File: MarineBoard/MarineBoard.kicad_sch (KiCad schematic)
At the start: 161 parts, among them CN1 MKDSN 1,5/ 2-5,08, CN2 MKDSN 1,5/ 2-5,08, CN3 SM04B-SRSS-TB (LF)(SN), CN4 BM10B-GHS-TBT, J1 USB_C_Receptacle_USB2.0_16P, Q2 S8050, Q3 S8050, Q4 BUK762R4-60E, U1 SY8089A1AAC, U11 SN65HVD230DR, U12 DB125-3.5-3P-GN-S, U13 DB125-3.5-3P-GN-S, U14 PC817C-S, U16 PC817C-S, U17 PC817C-S, U18 INA226, U19 INA226, U2 INA226, U21 PC817C-S, U22 SN74LVC1G14DBVR, U23 MCP1407-E/MF_C640313, U3 TPS5430DDA, U4 DB125-3.5-2P-GN-S, U5 DB125-3.5-2P-GN-S, U6 DB125-3.5-2P-GN-S, U7 DB125-3.5-3P-GN-S, U8 ESP32-S3-WROOM-2-N32R16V, U9 DB125-3.5-3P-GN-S

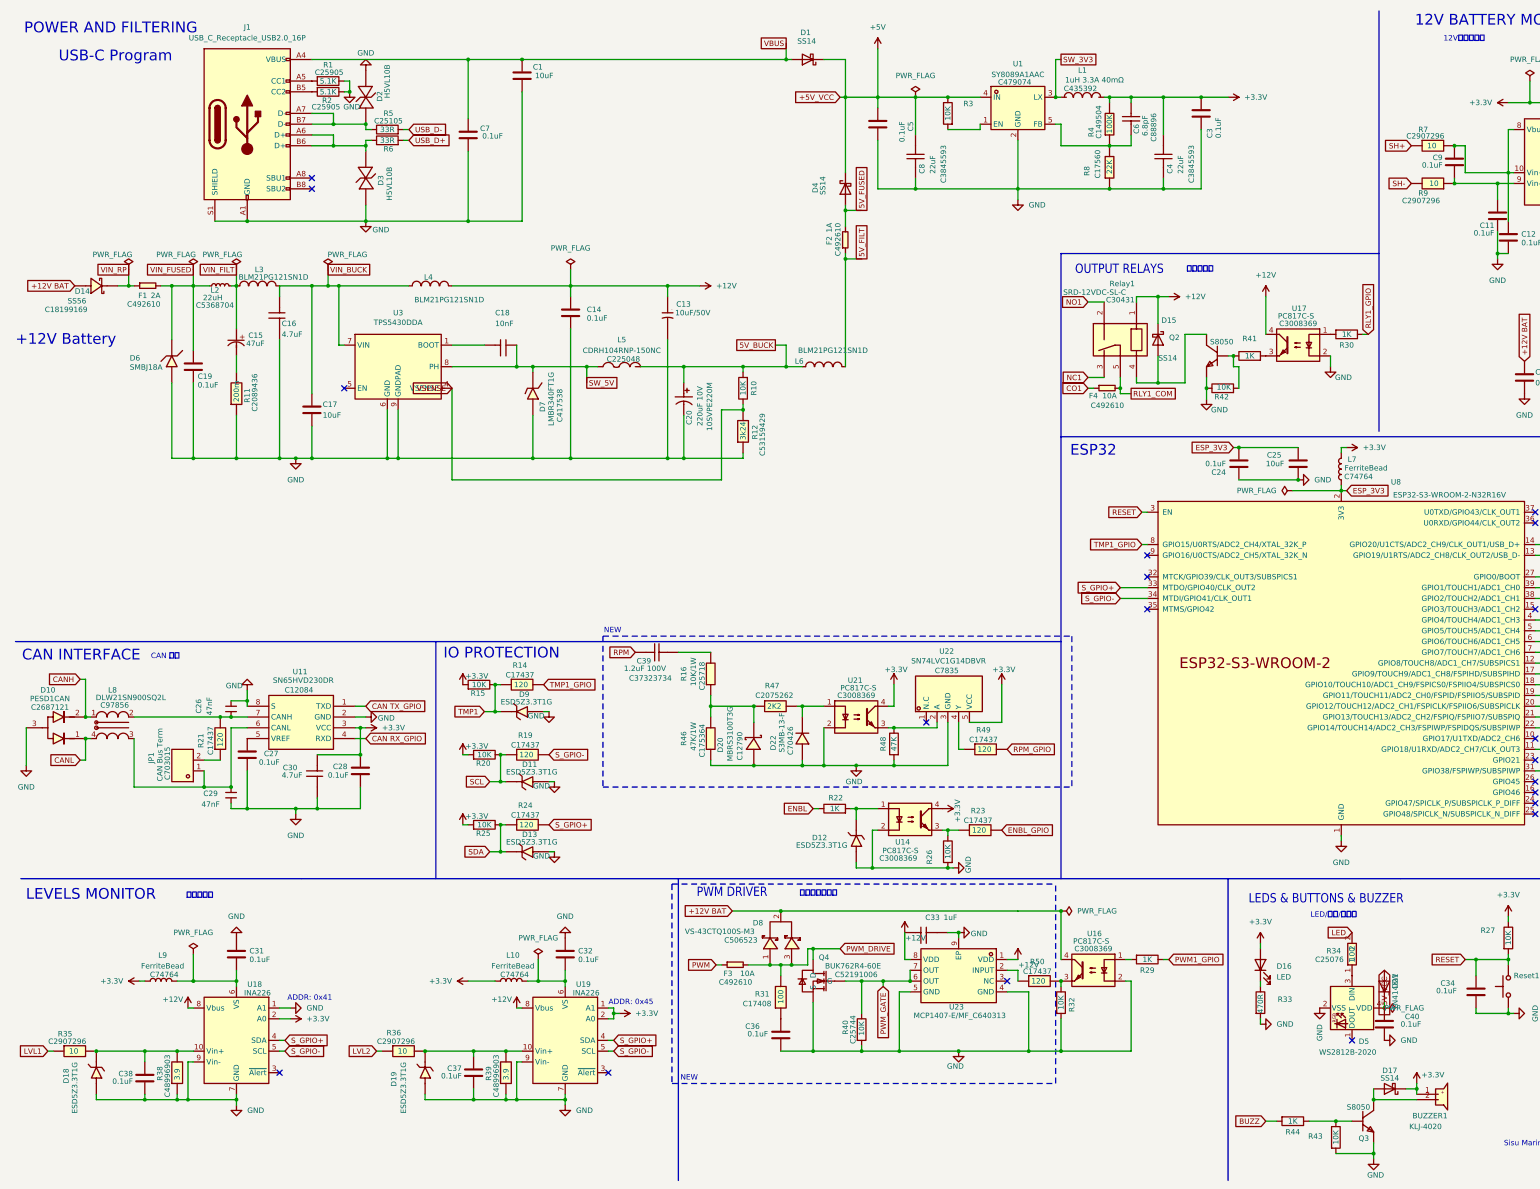
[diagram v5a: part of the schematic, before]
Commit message: MarineBoard: enclosure, PCBWay delivery, 5-unit BOM (#194)
Enclosure: printed PA12 box 129.4 x 107.9 x 44 mm, built by a parametric
FreeCAD script (enclosure/make_enclosure.py; fit_board.py checks the KiCad
board STEP against it). IP67 panel connectors with engraved legends
(EW-LP20 power/PWM, M12-5 CAN, 12G for TMP/RPM/ENBL, relay, shunt,
levels), 2 mm silicone-cord seal, D5 light pipe, 4 x M3x6 board and
4 x M3x10 lid screws, no USB opening (flash before boxing, then OTA).
STEP + STL exports, FreeCAD docs, render, and the PCBWay print/parts
order sheet. Documented in Technical Specs -> Enclosure; README,
INSTALLATION section 8.3 and Technical Specifications point to it.

Also: PCBWay's 15 Aug delivery package (design files, CAM, the earlier
enclosure, now marked superseded), the connector purchase list, and
the 5-unit assembly BOM. Order numbers are kept out of the file names.
Board BOM: real part numbers for generic parts (BLM21PG331SN1D,
KT-0603R, MCP1407-E/MF); production files regenerated; no copper change.
FreeCAD *.FCBak backups ignored. Project Claude permissions updated.

Signal K plugin configs stay uncommitted (local MQTT credentials).

Co-Authored-By: Claude Opus 5.5 <noreply@anthropic.com>
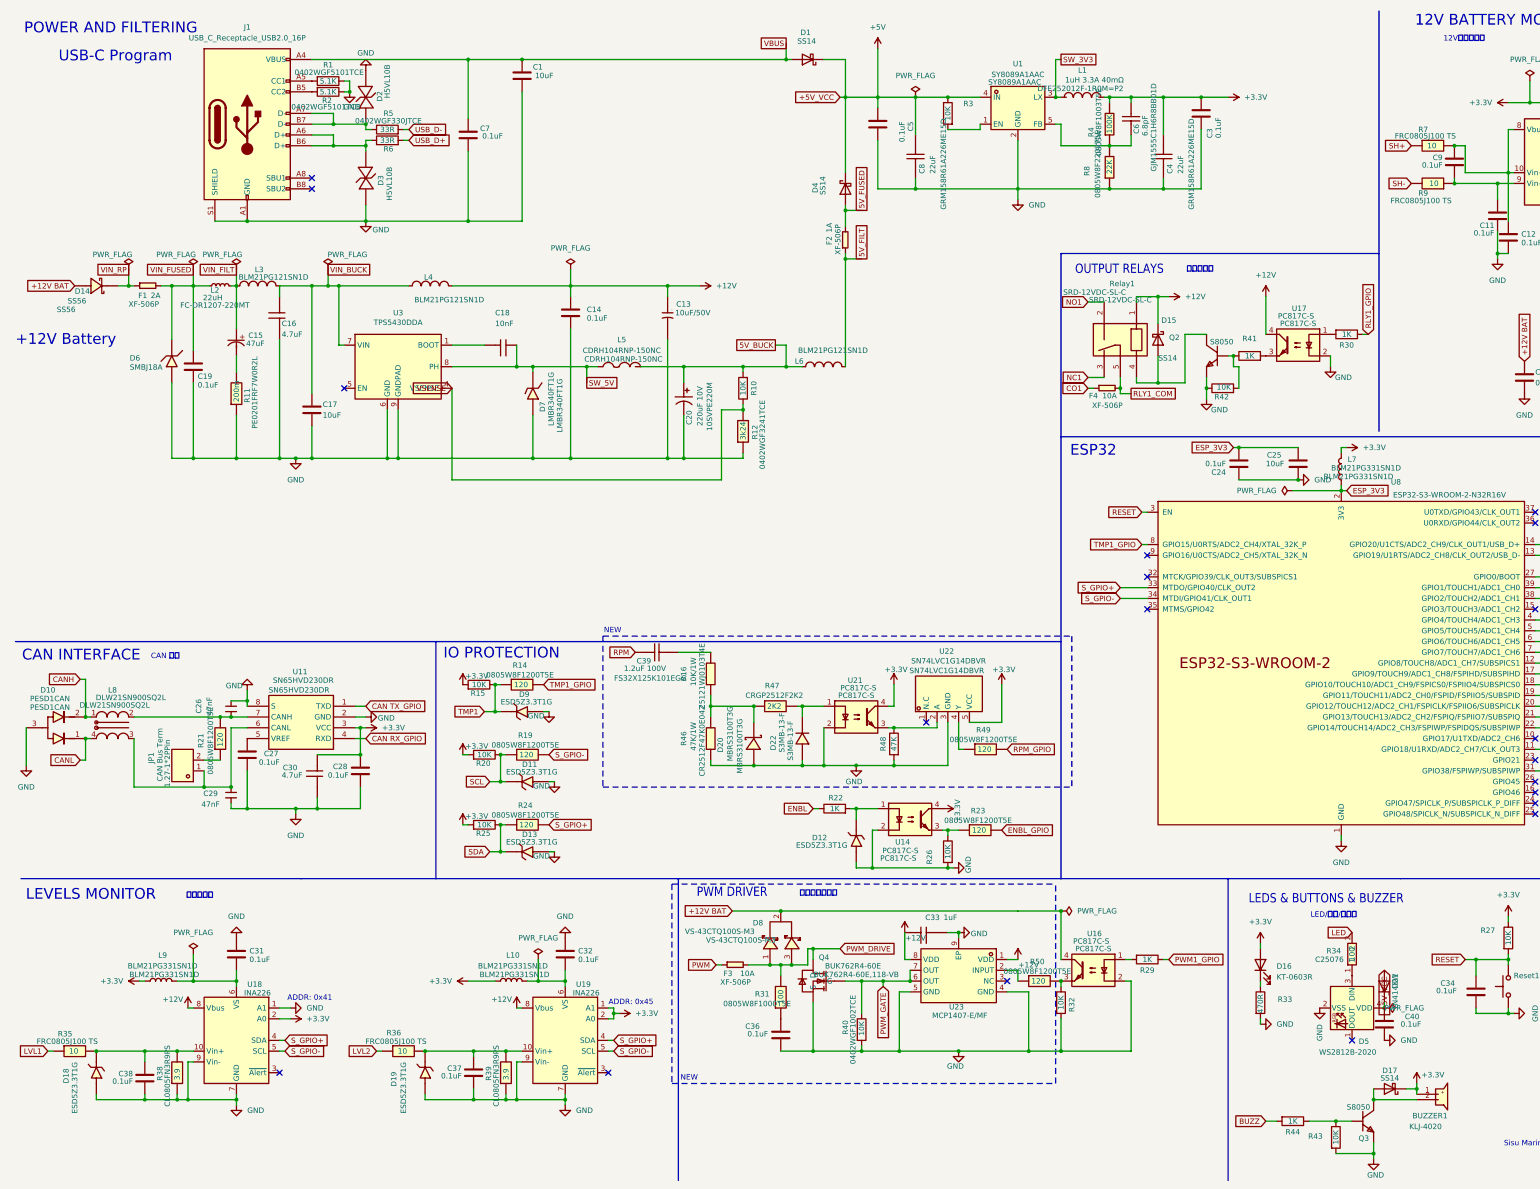
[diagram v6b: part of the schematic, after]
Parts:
- BUZZER1: MANUFACTURER (none) -> KELIKING
- C1, C11, C12, C14, C18, C19, C2, C24, C25, C27, C28, C3, C30, C31, C32, C34, C35, C36, C37, C38, C40, C42, C5, C7, C9: MANUFACTURER (none) -> Samsung Electro-Mechanics
- C13, C15, C26, C29, C33: MANUFACTURER (none) -> muRata
- C16: MANUFACTURER (none) -> Samsung Electro-Mechanics; MPN C51205 -> CL31B475KBHNNNE
- C17: MANUFACTURER (none) -> Samsung Electro-Mechanics; MPN C13585 -> CL31A106KBHNNNE
- C20: MANUFACTURER (none) -> Panasonic
- C39: MANUFACTURER (none) -> PSA; MPN C37323734 -> FS32X125K101EGG; Manufacturer Chinocera(华瓷) -> PSA
- C4, C8: MANUFACTURER (none) -> muRata; MPN C3845593 -> GRM158R61A226ME15D
- C6: MANUFACTURER (none) -> muRata; MPN C88896 -> GJM1555C1H6R8BB01D
- CN1, CN2: MANUFACTURER (none) -> Phoenix Contact
- CN3, CN4: MANUFACTURER (none) -> JST
- D1, D15, D17, D4: MANUFACTURER (none) -> onsemi; Manufacturer MDD(Microdiode Semiconductor) -> onsemi
- D10: MANUFACTURER (none) -> UMW; MPN C2687121 -> PESD1CAN; Manufacturer (none) -> UMW
- D11, D12, D13, D18, D19, D9: MANUFACTURER (none) -> onsemi; Manufacturer TECH PUBLIC -> onsemi
- D14: MANUFACTURER (none) -> R+O; MPN C18199169 -> SS56; Manufacturer R+O(宏嘉诚) -> R+O
- D16: value LED -> KT-0603R; MANUFACTURER (none) -> KENTO; MPN C2286 -> KT-0603R; Manufacturer (none) -> KENTO
- D2, D3: MANUFACTURER R+O(宏嘉诚) -> R+O; MPN C7420372 -> H5VL10B; Manufacturer (none) -> R+O
- D20: MANUFACTURER (none) -> onsemi; MPN C12790 -> MBRS3100T3G; Manufacturer onsemi(安森美) -> onsemi
- D21: MANUFACTURER (none) -> Diodes Incorporated
- D22: MANUFACTURER (none) -> Diodes Inc; MPN C70426 -> S3MB-13-F; Manufacturer DIODES(美台) -> Diodes Inc
- D5: MANUFACTURER (none) -> Worldsemi; MPN C52917434 -> WS2812B-2020
- D6: MANUFACTURER (none) -> Littelfuse; Manufacturer BORN -> Littelfuse
- D7: MANUFACTURER (none) -> LRC; MPN C417538 -> LMBR340FT1G; Manufacturer (none) -> LRC
- D8: MANUFACTURER (none) -> Vishay; MPN C506523 -> VS-43CTQ100S-M3; Manufacturer VISHAY(威世) -> Vishay
- F1, F2, F3, F4: MANUFACTURER (none) -> XFCN; MPN C492610 -> XF-506P; Manufacturer (none) -> XFCN
- Flash1, Reset1: MANUFACTURER (none) -> XKB; MPN C318884 -> TS-1187A-B-A-B; Manufacturer (none) -> XKB
- J1: MANUFACTURER (none) -> HCTL; MPN C2894897 -> HC-TYPE-C-16P-01A; Manufacturer (none) -> HCTL
- JP1: MANUFACTURER (none) -> BOOMELE; MPN C703015 -> 1.27-1*2PPin; Manufacturer (none) -> BOOMELE
- L1: MANUFACTURER (none) -> muRata; MPN C435392 -> DFE252012F-1R0M=P2; Manufacturer muRata(村田) -> muRata
- L10, L7, L9: value FerriteBead -> BLM21PG331SN1D; MANUFACTURER (none) -> muRata; MPN C74764 -> BLM21PG331SN1D; Manufacturer (none) -> muRata
- L2: MANUFACTURER (none) -> FANGCHENG; MPN C5368704 -> FC-DR1207-220MT; Manufacturer (none) -> FANGCHENG
- L3, L4, L6: MANUFACTURER muRata(村田) -> muRata; MPN C79382 -> BLM21PG121SN1D; Manufacturer (none) -> muRata
- L5: MANUFACTURER (none) -> Sumida; MPN C225048 -> CDRH104RNP-150NC; Manufacturer (none) -> Sumida
- L8: MANUFACTURER (none) -> muRata; MPN C97856 -> DLW21SN900SQ2L; Manufacturer (none) -> muRata
- Q2, Q3: MANUFACTURER 宏嘉诚 -> R+O; MPN C20069125 -> S8050; Manufacturer (none) -> R+O
- Q4: MANUFACTURER (none) -> VBsemi; MPN C52191006 -> BUK762R4-60E,118-VB; Manufacturer VBsemi(微碧半导体) -> VBsemi
- R1, R2: MANUFACTURER (none) -> UNI-ROYAL; MPN C25905 -> 0402WGF5101TCE; Manufacturer (none) -> UNI-ROYAL
- R10, R15, R20, R25, R26, R27, R28, R3, R32, R40, R42, R43: MANUFACTURER (none) -> UNI-ROYAL; MPN C25744 -> 0402WGF1002TCE; Manufacturer (none) -> UNI-ROYAL
- R11: MANUFACTURER (none) -> Yageo; MPN C2089436 -> PE0201FRF7W0R2L; Manufacturer (none) -> Yageo
- R12: MANUFACTURER (none) -> UNI-ROYAL; MPN C53159429 -> 0402WGF3241TCE; Manufacturer (none) -> UNI-ROYAL
- R14, R19, R21, R23, R24, R49, R50: MANUFACTURER (none) -> UNI-ROYAL; MPN C17437 -> 0805W8F1200T5E; Manufacturer (none) -> UNI-ROYAL
- R16: MANUFACTURER (none) -> UNI-ROYAL; MPN C25718 -> 25121WJ0103T4E; Manufacturer EVER OHMS(天二科技) -> UNI-ROYAL
- R22, R29, R30, R41, R44: MANUFACTURER (none) -> UNI-ROYAL; MPN C11702 -> 0402WGF1001TCE; Manufacturer (none) -> UNI-ROYAL
- R31: MANUFACTURER (none) -> UNI-ROYAL; MPN C17408 -> 0805W8F1000T5E; Manufacturer (none) -> UNI-ROYAL
- R33: MANUFACTURER (none) -> UNI-ROYAL; MPN C25117 -> 0402WGF4700TCE; Manufacturer (none) -> UNI-ROYAL
- R34: MANUFACTURER (none) -> UNI-ROYAL; Manufacturer UNI-ROYAL(厚声) -> UNI-ROYAL
- R35, R36, R7, R9: MANUFACTURER (none) -> FOJAN; MPN C2907296 -> FRC0805J100 TS; Manufacturer (none) -> FOJAN
- R38, R39: MANUFACTURER (none) -> Changlong; MPN C48996903 -> CL0805FN3R9PS; Manufacturer (none) -> Changlong
- R4: MANUFACTURER (none) -> UNI-ROYAL; MPN C149504 -> 0805W8F1003T5E; Manufacturer UNI-ROYAL(厚声) -> UNI-ROYAL
- R46: MANUFACTURER (none) -> EVER OHMS; MPN C175364 -> CR2512F47K0E04Z; Manufacturer EVER OHMS(天二科技) -> EVER OHMS
- R47: MANUFACTURER (none) -> TE Connectivity; MPN C2075262 -> CRGP2512F2K2; Manufacturer TE Connectivity(泰科电子) -> TE Connectivity
- R48: MANUFACTURER (none) -> UNI-ROYAL; MPN C25792 -> 0402WGF4702TCE; Manufacturer (none) -> UNI-ROYAL
- R5, R6: MANUFACTURER (none) -> UNI-ROYAL; MPN C25105 -> 0402WGF330JTCE; Manufacturer (none) -> UNI-ROYAL
- R8: MANUFACTURER (none) -> UNI-ROYAL; MPN C17560 -> 0805W8F2202T5E; Manufacturer UNI-ROYAL(厚声) -> UNI-ROYAL
- Relay1: MANUFACTURER (none) -> Songle; MPN C30431 -> SRD-12VDC-SL-C; Manufacturer (none) -> Songle
- U1: MANUFACTURER (none) -> Silergy; MPN C479074 -> SY8089A1AAC; Manufacturer Silergy(矽力杰) -> Silergy
- U11: MANUFACTURER (none) -> TI; MPN C12084 -> SN65HVD230DR; Manufacturer (none) -> TI
- U12, U13, U7, U9: MANUFACTURER (none) -> DORABO; MPN C466971 -> DB125-3.5-3P-GN-S; Manufacturer (none) -> DORABO
- U14, U16, U17, U21: MANUFACTURER (none) -> UMW; MPN C3008369 -> PC817C-S; Manufacturer (none) -> UMW
- U18, U19, U2: MANUFACTURER (none) -> TI
- U22: MANUFACTURER (none) -> TI; MPN C7835 -> SN74LVC1G14DBVR; Manufacturer TI(德州仪器) -> TI
- U23: value MCP1407-E/MF_C640313 -> MCP1407-E/MF; MANUFACTURER (none) -> Microchip; MPN C640313 -> MCP1407-E/MF; Manufacturer MICROCHIP(美国微芯) -> Microchip
- U3: MANUFACTURER (none) -> TI; MPN C502477 -> TPS5430DDA; Manufacturer (none) -> TI
- U4, U5, U6: MANUFACTURER (none) -> DORABO; MPN C466970 -> DB125-3.5-2P-GN-S; Manufacturer (none) -> DORABO
- U8: MANUFACTURER (none) -> Espressif; MPN C42417293 -> ESP32-S3-WROOM-2-N32R16V; Manufacturer (none) -> Espressif
